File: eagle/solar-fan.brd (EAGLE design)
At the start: 92 x 19.7 mm, 44 parts, among them J1 POWER_JACKPTH, J3 7805, J6 USB_, U1 LT3652, U2 ATTINY85

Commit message: rev - build
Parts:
- removed LOGO1: OSHW-LOGOMINI, SparkFun-Aesthetics:OSHW-LOGO-MINI
- added D10: BZX84C6V2L, SparkFun-DiscreteSemi:SOT23-3
- C1, C4: device SparkFun-Passives:1210 -> SparkFun-Passives:0603-CAP
- C2: value 4.7uf -> 10uf
- C6: value 0.1uf -> 10uf
- C7: value 0.33uf -> 10uf
- D2: value BZX84C6V2L -> 1N914; device SparkFun-DiscreteSemi:SOT23-3 -> SparkFun-DiscreteSemi:SOD-323
- D3: value MBRS340 -> MBRS140
- L1: value 22uH -> 10uH
- R13, R14, R15: value 100k -> 390
- moved JP1 58.4 mm to (83.2, 6.35), turned to 0 degrees
- moved R9 8.89 mm to (60.3, 16.5), turned to 180 degrees
- moved R11 3.81 mm to (51.4, 16.5), turned to 0 degrees
- moved D1 3.70 mm to (14.0, 9.53), turned to 90 degrees
- moved D2 3.42 mm to (20.3, 17.1)
- moved D9 2.01 mm to (48.3, 16.5), turned to 180 degrees
- moved R10 1.91 mm to (60.3, 14.6)
- moved C1 1.80 mm to (17.1, 11.4)
- moved C2 1.42 mm to (17.1, 8.26), turned to 180 degrees
- moved D7 1.27 mm to (45.1, 14.6)
- moved D8 1.27 mm to (45.1, 12.7)
- moved R12 1.27 mm to (45.1, 16.5), turned to 180 degrees
- moved D3 1.27 mm to (24.1, 17.8)
- moved R4 1.27 mm to (29.2, 5.08)
- moved C6 1.27 mm to (41.9, 14.0)
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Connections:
- removed net N$20: J6.D+, J6.D-
- new net N$10: D10.1, D2.A
- new net N$8: J6.D+, JP1.1
- new net N$9: J6.D-, JP1.2
- net BOOST: now also D2.C; no longer D2.1
- net GND: no longer JP1.1
- net PAD: no longer JP1.2
- net V_BATT: now also D10.3; no longer D2.3
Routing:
- net N$10: track 0.00 -> 8.01 mm
- net VBAT: track 13.4 -> 6.40 mm
- net SHDN: track 18.2 -> 12.8 mm
- net BOOST: track 5.69 -> 10.9 mm
- net SW: track 10.8 -> 15.8 mm
- net N$9: track 0.00 -> 3.18 mm
- net N$8: track 0.00 -> 3.18 mm
- net PAD: track 2.73 -> 0.00 mm
- net SENSE: track 13.8 -> 11.1 mm
- net N$18: track 3.25 -> 5.64 mm
- net N$20: track 2.00 -> 0.00 mm
- net FAN_IN: track 8.70 -> 7.00 mm
- net GND: track 20.3 -> 21.3 mm, vias 5 -> 6
- net N$19: track 12.4 -> 13.4 mm
- net N$7: track 11.1 -> 12.0 mm
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- added copper zone on layer 1, net GND
- added copper zone on layer 1, net PAD
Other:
- board text added: "danwahl.net/"
- board text added: "rev - | sn:"
- board text removed: "danwahl.net | 2016"
- board text removed: "rev - | sn"

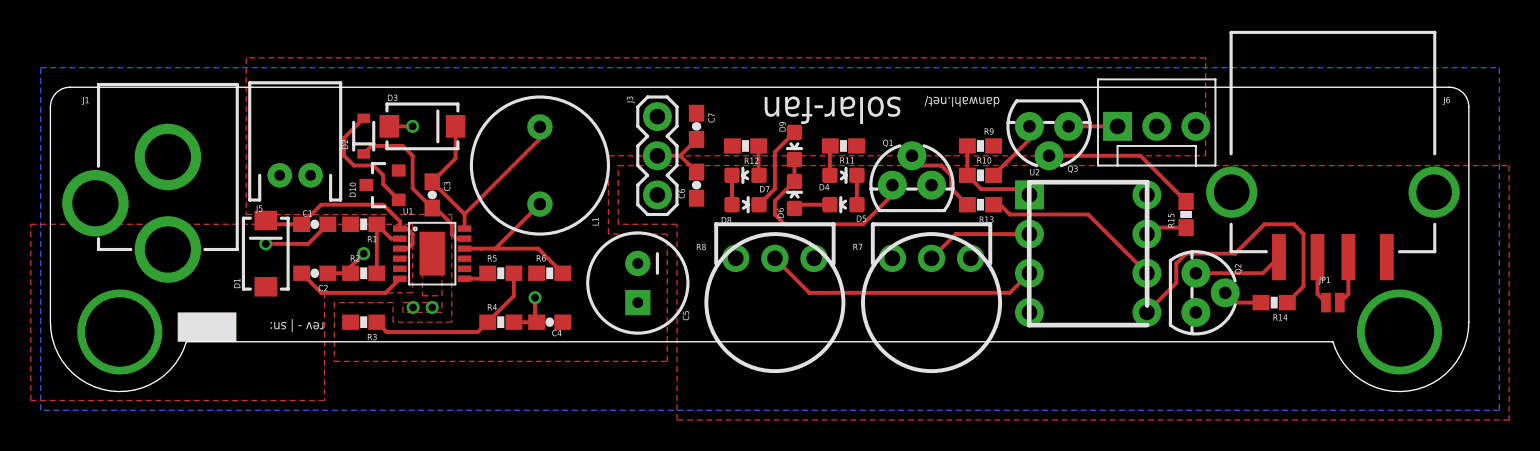
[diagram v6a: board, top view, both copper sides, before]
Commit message: - updated charge voltage - led/cap placement - proper fan vs. usb out on micro - changed transistors to smd - solder mask change for gnd pad - added status leds for chager - changed battery/solar connectors
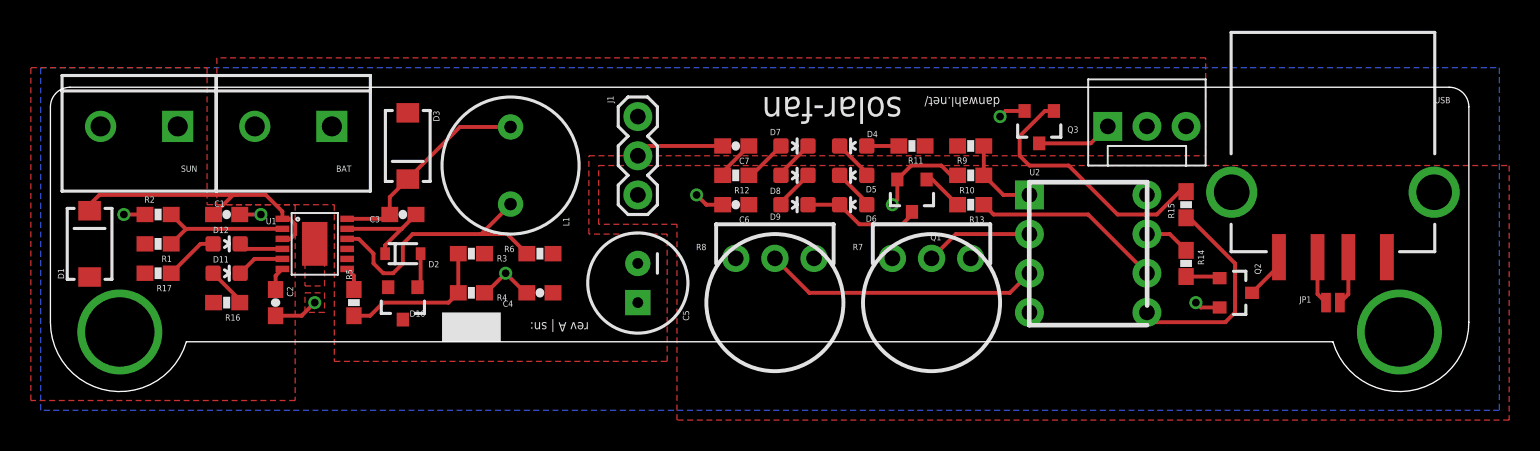
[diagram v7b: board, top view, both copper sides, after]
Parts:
- removed J2: (no value), SparkFun-Connectors:MOLEX-1X3
- removed J3: 7805, SparkFun-Connectors:1X03
- removed J5: (no value), SparkFun-Connectors:JST-2-PTH
- added BAT, SUN: (no value), SparkFun-Connectors:SCREWTERMINAL-5MM-2
- added D11, D12: (no value), SparkFun-LED:LED-0603
- added FAN: (no value), SparkFun-Connectors:MOLEX-1X3
- added R16, R17: 100, SparkFun-Passives:0603-RES
- J1: value POWER_JACKPTH -> 7805; device SparkFun-Connectors:POWER_JACK_PTH -> SparkFun-Connectors:1X03
- Q1, Q2, Q3: value (none) -> MMBT2222A; device SparkFun-DiscreteSemi:TO-92 -> SparkFun-DiscreteSemi:SOT23-3
- R1: value 499k -> 430k
- R10: value 100k -> 1k
- R9: value 309k -> 2.2k
- moved J1 30.9 mm to (38.1, 18.4), turned to 270 degrees
- moved R2 13.9 mm to (6.99, 12.1)
- moved R1 13.4 mm to (6.99, 10.2)
- moved D1 11.4 mm to (2.54, 10.2)
- moved R5 9.71 mm to (19.7, 6.35), turned to 270 degrees
- moved R3 8.28 mm to (27.3, 9.53), turned to 0 degrees
- moved D2 8.03 mm to (22.9, 9.53), turned to 0 degrees
- moved D10 7.73 mm to (22.9, 6.35), turned to 180 degrees
- moved U1 7.65 mm to (17.1, 10.2)
- moved R14 6.25 mm to (73.7, 8.89), turned to 270 degrees
- moved C1 5.75 mm to (11.4, 12.1)
- moved R11 4.45 mm to (55.9, 16.5)
- moved D6 3.86 mm to (52.1, 12.7), turned to 90 degrees
- moved D9 3.81 mm to (48.3, 12.7), turned to 270 degrees
- moved D7 3.70 mm to (48.3, 16.5), turned to 270 degrees
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- renumbered J6 to USB
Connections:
- new net N$11: D12.A, R17.1
- new net N$12: D12.C, U1.4
- new net N$20: D11.C, U1.5
- new net N$22: D11.A, R16.1
- net 5V: now also J1.3; no longer J3.3
- net FAN_OUT: now also U2.5; no longer U2.7
- net GND: now also BAT.1, J1.2, Q1.2, Q2.2, Q3.2, SUN.1; no longer J1.GND, J3.2, J5.1, Q1.3, Q2.3, Q3.3
- net N$1: now also Q1.1; no longer Q1.2
- net N$19: now also Q1.3; no longer Q1.1
- net N$2: now also Q2.1; no longer Q2.2
- net N$21: now also Q2.3; no longer Q2.1
- net N$3: now also Q3.1; no longer Q3.2
- net N$6: now also FAN.1, Q3.3; no longer J2.1, Q3.1
- net USB_OUT: now also U2.7; no longer U2.5
- net VIN: now also R16.2, R17.2, SUN.2; no longer J1.PWR
- net V_BATT: now also BAT.2, FAN.2, J1.1; no longer J2.2, J3.1, J5.2
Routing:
- net USB_OUT: track 18.4 -> 2.98 mm
- net FAN_OUT: track 2.71 -> 13.8 mm
- net N$3: track 10.1 -> 17.2 mm
- net SENSE: track 11.1 -> 18.0 mm
- net GND: track 21.3 -> 27.1 mm, vias 6 -> 8
- net TIMER: track 7.28 -> 1.52 mm
- net N$10: track 8.01 -> 2.26 mm
- net N$19: track 13.4 -> 7.70 mm
- net SHDN: track 12.8 -> 18.4 mm
- net VIN_REG: track 5.06 -> 9.44 mm
- net BOOST: track 10.9 -> 7.35 mm
- net N$11: track 0.00 -> 3.51 mm
- net N$20: track 0.00 -> 3.12 mm
- net N$18: track 5.64 -> 2.63 mm
- net N$12: track 0.00 -> 2.87 mm
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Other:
- board text added: "rev A | sn:"
- board text removed: "rev - | sn:"

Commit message: rev A build
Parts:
- added F1: PTC0603, SparkFun-PowerIC:0603
- R16, R17: value 100 -> 10K
- moved C2 2.01 mm to (12.7, 5.71)
- moved R16 1.71 mm to (9.84, 5.71), turned to 270 degrees
- moved R5 1.59 mm to (20.6, 5.08), turned to 0 degrees
- moved U1 1.27 mm to (17.1, 8.89)
- moved D10 0.71 mm to (23.2, 6.99)
- moved D2 0.71 mm to (23.2, 10.2)
- moved C3 0.32 mm to (23.2, 12.1)
- turned L1 to 180 degrees
- renumbered J1 to +5V
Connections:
- new net N$23: BAT.2, F1.1
- net V_BATT: now also F1.2; no longer BAT.2
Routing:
- net N$23: track 0.00 -> 6.97 mm
- net GND: track 27.1 -> 33.0 mm
- net SW: track 13.7 -> 10.9 mm
- net BOOST: track 7.35 -> 5.64 mm
- net N$7: track 9.93 -> 8.30 mm
- net TIMER: track 1.52 -> 2.63 mm
- net SHDN: track 18.4 -> 19.5 mm
- net N$12: track 2.87 -> 3.86 mm
- net VFB: track 1.52 -> 2.41 mm
- net N$22: track 2.66 -> 2.02 mm
- net SENSE: track 18.0 -> 18.5 mm
- net VIN_REG: track 9.44 -> 9.94 mm
